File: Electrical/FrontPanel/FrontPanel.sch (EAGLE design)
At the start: 24 parts, among them SW1 EC12E_SW

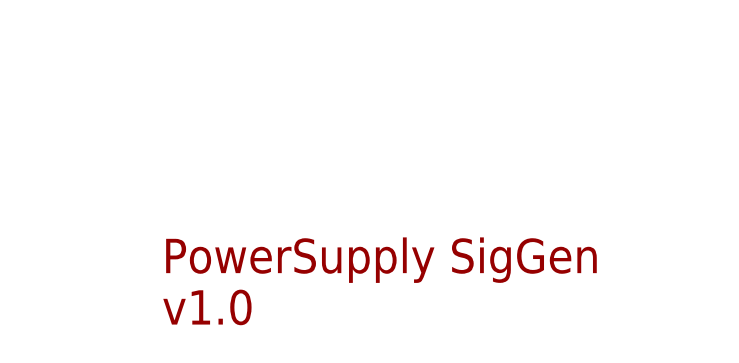
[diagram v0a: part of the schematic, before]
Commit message: Updated to new project name (PS_Fgen_HW), removed Z-Diode and ATX_PWR_ON signal from MainBoard
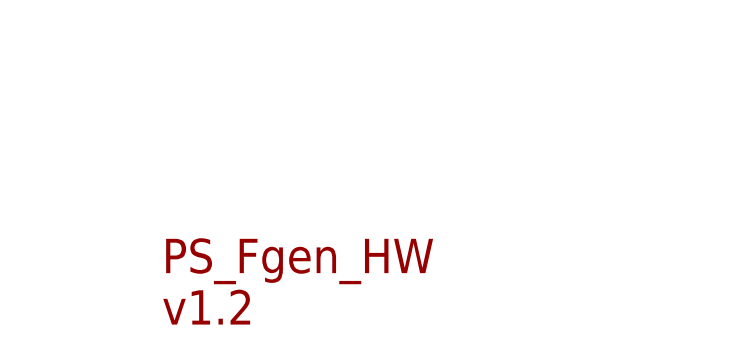
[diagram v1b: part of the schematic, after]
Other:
- note added: "PS_Fgen_HW v1.2"
- note removed: "PowerSupply SigGen v1.0"
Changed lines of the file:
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@@
 <?xml version="1.0" encoding="utf-8"?>
 <!DOCTYPE eagle SYSTEM "eagle.dtd">
-<eagle version="9.5.2">
+<eagle version="9.6.2">
 <drawing>
 <settings>
@@
 <sheet>
 <plain>
-<text x="162.56" y="22.86" size="3.81" layer="94" align="top-left">PowerSupply SigGen
-v1.0</text>
+<text x="162.56" y="22.86" size="3.81" layer="94" align="top-left">PS_Fgen_HW
+v1.2</text>
 <text x="27.94" y="86.36" size="3.81" layer="97">Keypad</text>
 <text x="88.9" y="157.48" size="3.81" layer="97">Encoder</text>
